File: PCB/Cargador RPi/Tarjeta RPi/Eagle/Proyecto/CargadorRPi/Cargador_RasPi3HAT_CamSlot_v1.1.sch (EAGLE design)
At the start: 22 parts, among them J2 PIN20X2, U1 MCP3208, X2 22-23-2081

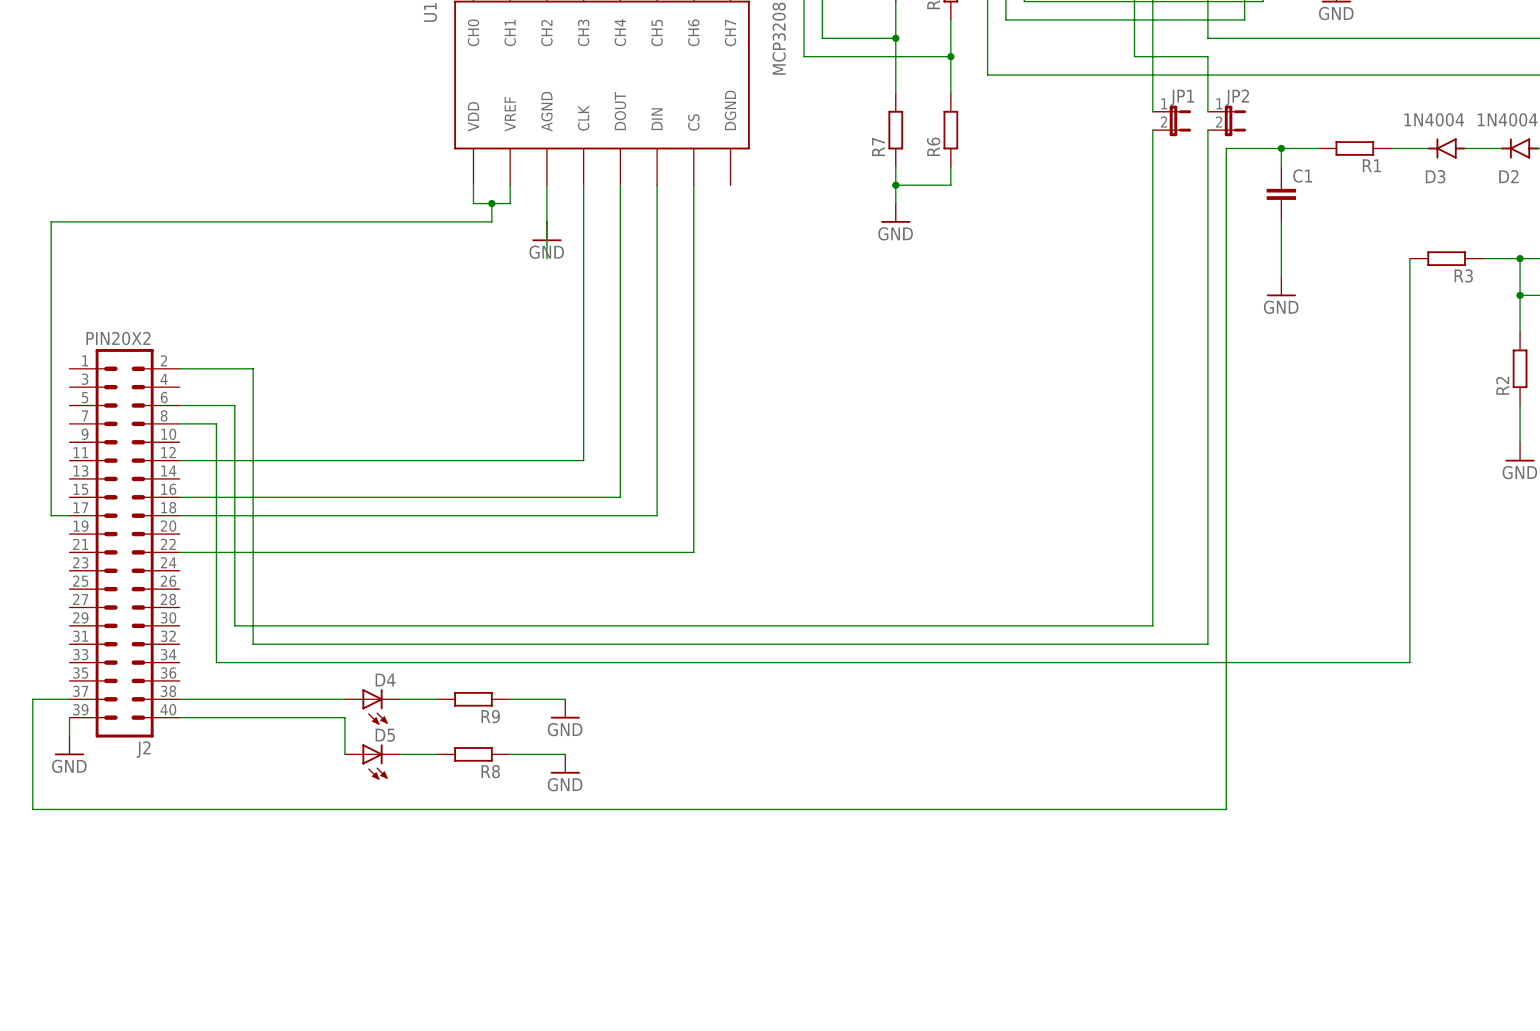
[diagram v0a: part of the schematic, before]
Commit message: Ajustes para fabricación de PCB.
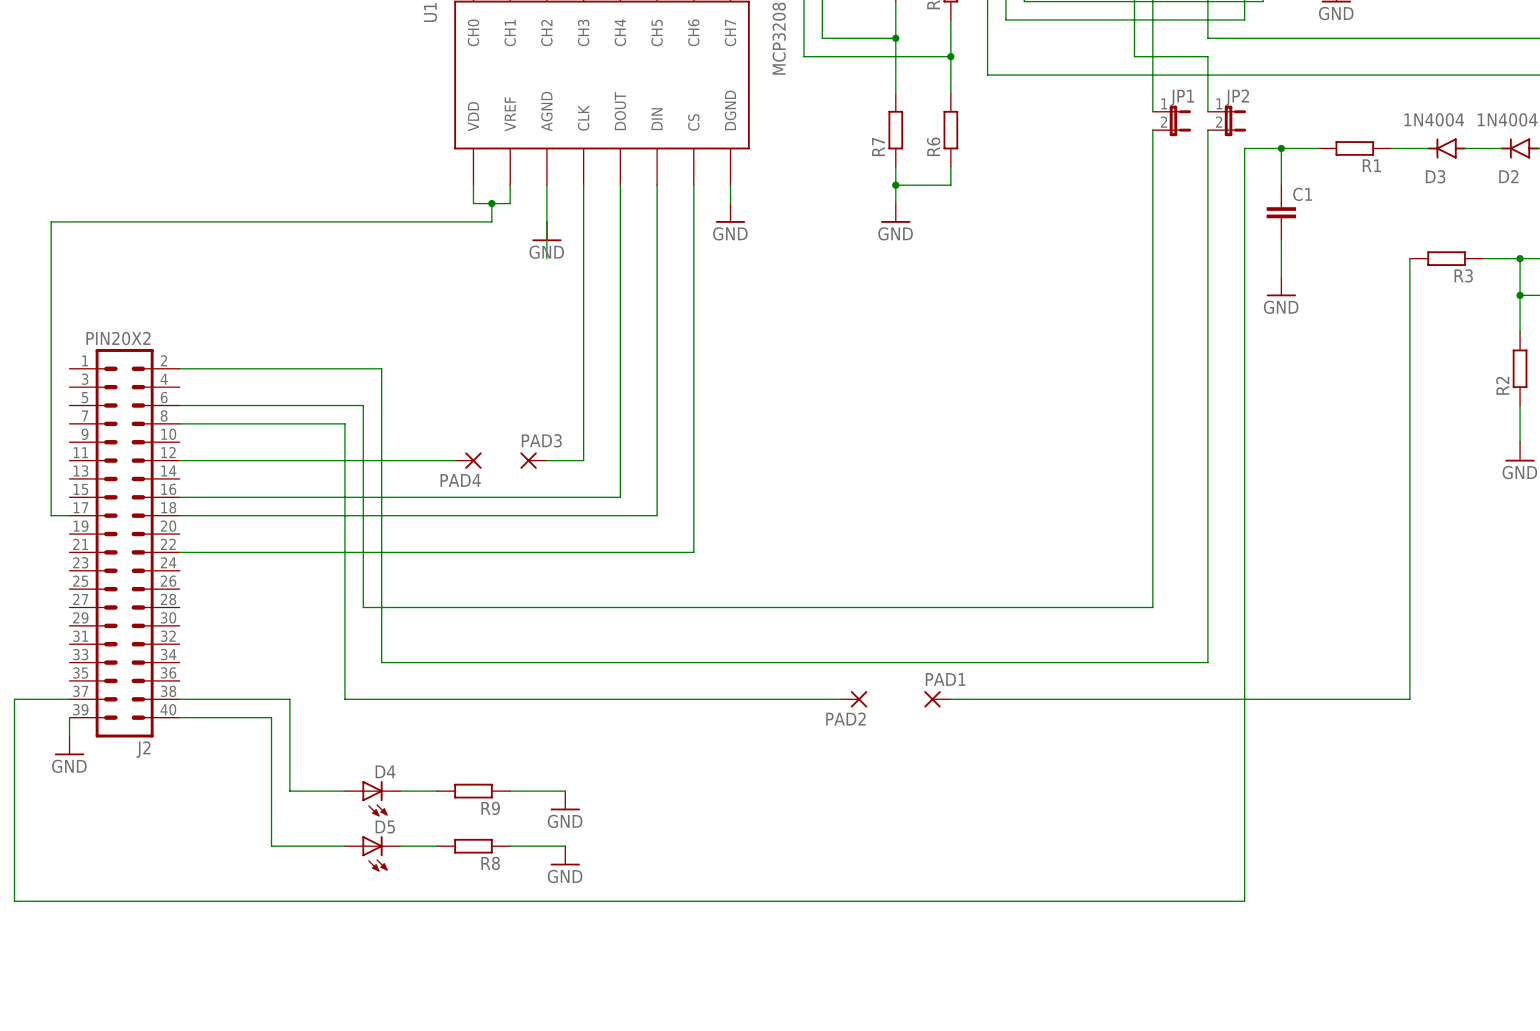
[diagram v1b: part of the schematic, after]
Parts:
- added PAD1, PAD2, PAD3, PAD4: (no value), wirepad:2,15/1,0
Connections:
- new net N$20: PAD3.P, U1.CLK
- new net N$8: J2.12, PAD4.P
- net GND: now also U1.DGND
- net N$11: now also PAD1.P, R3.2; no longer J2.12, U1.CLK
- net N$2: now also PAD2.P; no longer R3.2
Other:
- moved on the sheet: C1, D4, D5, R8, R9
